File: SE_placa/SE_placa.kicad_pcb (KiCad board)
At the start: 2 copper layers, 118.1 x 58.4 mm, 70 parts, among them IC1 TP4056, J1 5V, J2 Micro_SD_Card_Det_Hirose_DM3AT, J3 Conn_02x07_ESP32_IO, J4 I2C-0, J5 I2C-1, J6 Conn_02x03_LORA_IO, J7 U.FL-R-SMT(01), J8 UART, J9 Connector Bateria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

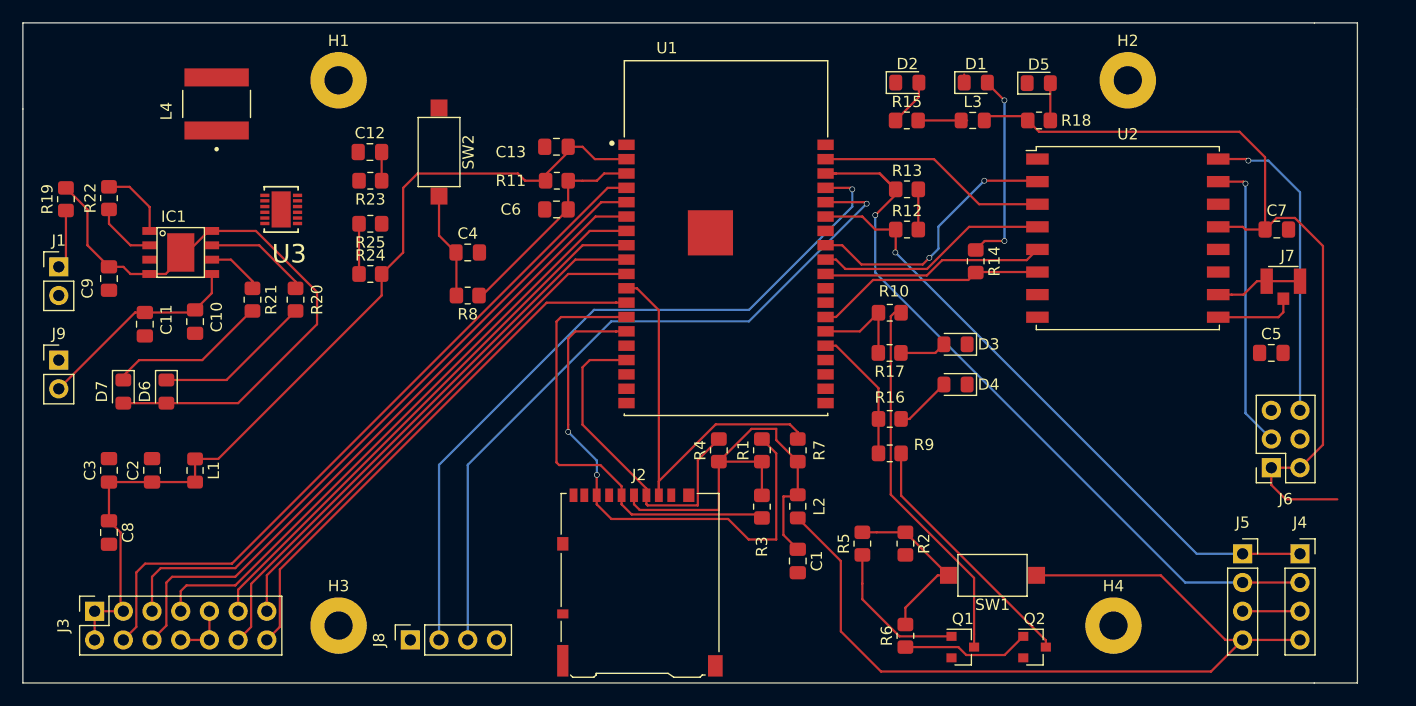
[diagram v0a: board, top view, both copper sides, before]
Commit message: continuacion de ruteo
Solo queda por rutear tierras.
agrego regla de ruteo para el U3 elemento mas pequeño regulador LTC3441, aun siguen generando error la base del elemento.
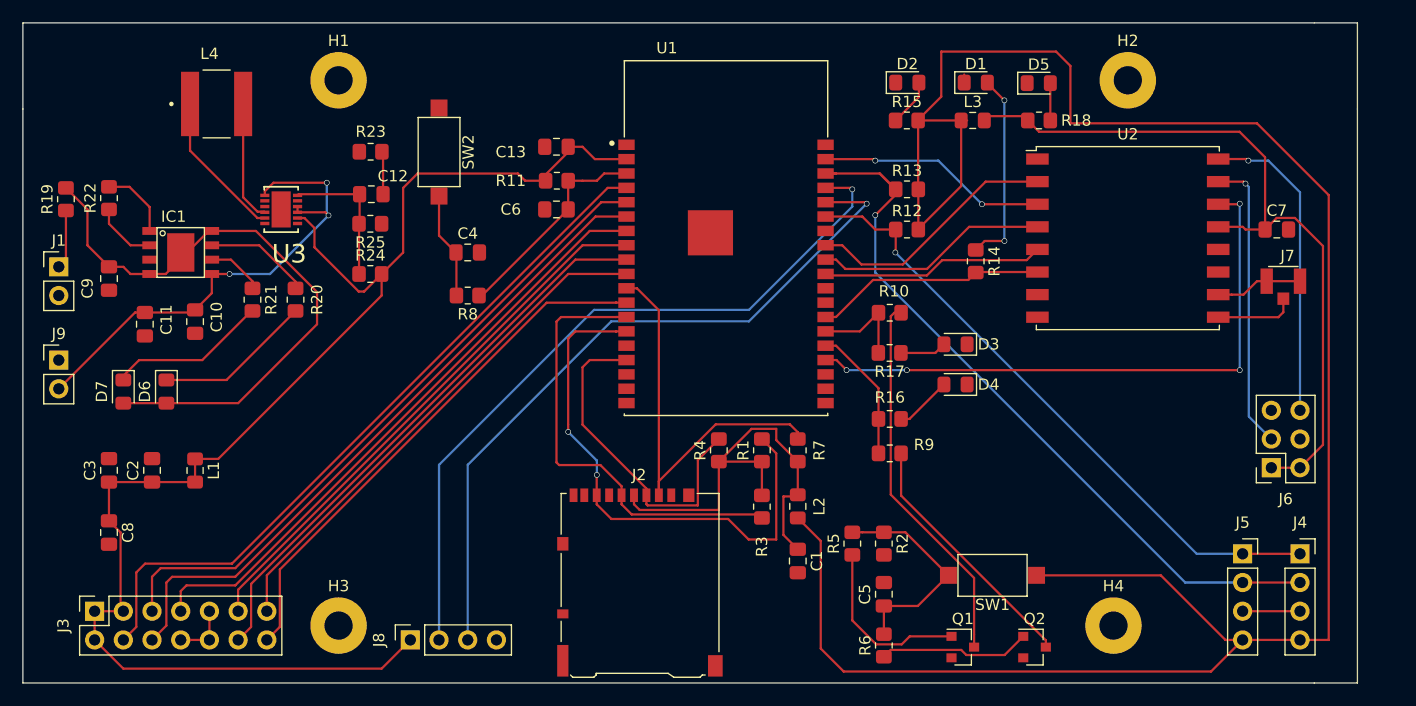
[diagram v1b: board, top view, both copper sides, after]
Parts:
- moved C5 40.4 mm to (177.8, 68.3), turned to 90 degrees
- moved C12 3.74 mm to (132.4, 32.9)
- moved R23 2.57 mm to (132.4, 29.2)
- moved R6 2.09 mm to (177.8, 72.9)
- moved R2 1.91 mm to (177.8, 63.9)
- moved R5 0.89 mm to (175.0, 63.9)
- turned L4 to 0 degrees
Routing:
- net +3V3: track 165.7 -> 318.4 mm
- net Net-(U1-Pad23): track 0.00 -> 53.7 mm, vias 0 -> 4
- net /cargador_regulador/BAT+: track 18.7 -> 43.7 mm, vias 0 -> 3
- net Net-(L4-Pad1): track 0.00 -> 13.2 mm
- net Net-(L4-Pad2): track 0.00 -> 10.7 mm
- net /cargador_regulador/FB: track 4.45 -> 12.6 mm
- net +3.3VP: track 74.5 -> 66.6 mm
- net Net-(C5-Pad1): track 15.7 -> 19.4 mm
- net Net-(Q1-Pad1): track 13.2 -> 15.7 mm
- net Net-(Q2-Pad1): track 11.4 -> 13.5 mm
- net Net-(C12-Pad2): track 2.54 -> 3.80 mm
- net Net-(U1-Pad31): track 23.7 -> 22.5 mm, vias 2 -> 0
- net Net-(U1-Pad37): vias 0 -> 2
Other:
- net class U3 added: clearance 0.2, trace_width 0.2, via_dia 0.4, via_drill 0.3
- rule trace_min: 0.2 -> 0.15

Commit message: ruteo de tierras
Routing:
- net GND: track 25.5 -> 392.2 mm
- net Net-(R23-Pad2): track 0.00 -> 9.23 mm, vias 0 -> 2
- net Net-(U1-Pad23): track 53.7 -> 56.4 mm
- net /cargador_regulador/BAT+: track 43.7 -> 44.6 mm
- net /SPI2-SCK: track 40.0 -> 39.4 mm

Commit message: actualizacion tierra
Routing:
- net GND: track 392.2 -> 442.2 mm, vias 0 -> 4
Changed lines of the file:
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@@
     (thickness 1.6)
     (drawings 8)
-    (tracks 514)
+    (tracks 540)
     (zones 0)
     (modules 70)
@@
   (segment (start 143.51 72.39) (end 147.54 72.39) (width 0.2) (layer F.Cu) (net 1))
   (segment (start 170.18 67.39) (end 162.885 74.685) (width 0.2) (layer F.Cu) (net 1))
-  (segment (start 170.18 66.4425) (end 170.18 67.39) (width 0.2) (layer F.Cu) (net 1))
   (segment (start 170.18 66.4425) (end 164.2325 66.4425) (width 0.2) (layer F.Cu) (net 1))
   (segment (start 161.675 63.885) (end 149.385 63.885) (width 0.2) (layer F.Cu) (net 1))
@@
   (segment (start 153.485 57.6) (end 153.035 57.15) (width 0.2) (layer F.Cu) (net 1))
   (segment (start 153.485 59.585) (end 153.485 57.6) (width 0.2) (layer F.Cu) (net 1))
+  (segment (start 215.265 37.719) (end 213.614 36.068) (width 0.2) (layer F.Cu) (net 1))
+  (segment (start 215.265 40.005) (end 215.265 37.719) (width 0.2) (layer F.Cu) (net 1))
+  (segment (start 214.63 40.64) (end 215.265 40.005) (width 0.2) (layer F.Cu) (net 1))
+  (segment (start 189.535 74.575) (end 190.135 73.975) (width 0.2) (layer F.Cu) (net 1))
+  (segment (start 184.435 74.575) (end 189.535 74.575) (width 0.2) (layer F.Cu) (net 1))
+  (segment (start 183.835 73.975) (end 184.435 74.575) (width 0.2) (layer F.Cu) (net 1))
+  (segment (start 183.785 73.975) (end 183.835 73.975) (width 0.2) (layer F.Cu) (net 1))
+  (via (at 179.705 74.295) (size 0.5) (drill 0.4) (layers F.Cu B.Cu) (net 1))
+  (segment (start 180.025 73.975) (end 179.705 74.295) (width 0.2) (layer F.Cu) (net 1))
+  (segment (start 183.785 73.975) (end 180.025 73.975) (width 0.2) (layer F.Cu) (net 1))
+  (via (at 179.705 67.945) (size 0.5) (drill 0.4) (layers F.Cu B.Cu) (net 1))
+  (segment (start 179.705 74.295) (end 179.705 67.945) (width 0.2) (layer B.Cu) (net 1))
+  (segment (start 178.435 67.945) (end 177.8 67.31) (width 0.2) (layer F.Cu) (net 1))
+  (segment (start 179.705 67.945) (end 178.435 67.945) (width 0.2) (layer F.Cu) (net 1))
+  (via (at 175.26 67.31) (size 0.5) (drill 0.4) (layers F.Cu B.Cu) (net 1))
+  (segment (start 177.8 67.31) (end 175.26 67.31) (width 0.2) (layer F.Cu) (net 1))
+  (via (at 171.45 67.945012) (size 0.5) (drill 0.4) (layers F.Cu B.Cu) (net 1))
+  (segment (start 172.085012 67.31) (end 171.45 67.945012) (width 0.2) (layer B.Cu) (net 1))
+  (segment (start 175.26 67.31) (end 172.085012 67.31) (width 0.2) (layer B.Cu) (net 1))
+  (segment (start 170.815012 67.945012) (end 170.18 67.31) (width 0.2) (layer F.Cu) (net 1))
+  (segment (start 171.45 67.945012) (end 170.815012 67.945012) (width 0.2) (layer F.Cu) (net 1))
+  (segment (start 170.18 67.31) (end 170.18 67.39) (width 0.2) (layer F.Cu) (net 1))
+  (segment (start 170.18 66.4425) (end 170.18 67.31) (width 0.2) (layer F.Cu) (net 1))
+  (segment (start 192.04 43.18) (end 191.39 43.83) (width 0.2) (layer F.Cu) (net 1))
+  (segment (start 205.105 43.18) (end 192.04 43.18) (width 0.2) (layer F.Cu) (net 1))
+  (segment (start 206.455 41.83) (end 205.105 43.18) (width 0.2) (layer F.Cu) (net 1))
+  (segment (start 207.39 41.83) (end 206.455 41.83) (width 0.2) (layer F.Cu) (net 1))
   (segment (start 167.005 59.595) (end 167.005 56.61) (width 0.2) (layer F.Cu) (net 2))
   (segment (start 167.005 56.61) (end 163.195 56.61) (width 0.2) (layer F.Cu) (net 2))
@@
   (segment (start 185.785 66.904998) (end 185.785 71.882001) (width 0.2) (layer F.Cu) (net 25))
   (segment (start 185.785 71.882001) (end 185.785 73.025) (width 0.2) (layer F.Cu) (net 25))
-  (segment (start 179.37899 72.78201) (end 180.086 72.075) (width 0.2) (layer F.Cu) (net 26))
-  (segment (start 177.122176 72.78201) (end 179.37899 72.78201) (width 0.2) (layer F.Cu) (net 26))
-  (segment (start 180.086 72.075) (end 183.785 72.075) (width 0.2) (layer F.Cu) (net 26))
-  (segment (start 175.006 70.665834) (end 177.122176 72.78201) (width 0.2) (layer F.Cu) (net 26))
-  (segment (start 175.006 64.865) (end 175.006 70.665834) (width 0.2) (layer F.Cu) (net 26))
+  (segment (start 175.006 64.865) (end 174.709998 65.161002) (width 0.2) (layer F.Cu) (net 26))
+  (segment (start 174.709998 65.161002) (end 174.709998 70.369832) (width 0.2) (layer F.Cu) (net 26))
+  (segment (start 174.709998 70.369832) (end 177.122176 72.78201) (width 0.2) (layer F.Cu) (net 26))
+  (segment (start 177.122176 72.78201) (end 183.07799 72.78201) (width 0.2) (layer F.Cu) (net 26))
+  (segment (start 183.07799 72.78201) (end 183.785 72.075) (width 0.2) (layer F.Cu) (net 26))
   (segment (start 179.324 59.614) (end 192.135 72.425) (width 0.2) (layer F.Cu) (net 27))
   (segment (start 179.324 55.88) (end 179.324 59.614) (width 0.2) (layer F.Cu) (net 27))
@@
     (polygon
       (pts
-        (xy 205.74 44.45) (xy 193.04 44.45) (xy 193.04 27.94) (xy 205.74 27.94)
+        (xy 205.74 40.64) (xy 193.04 40.64) (xy 193.04 27.94) (xy 205.74 27.94)
       )
     )

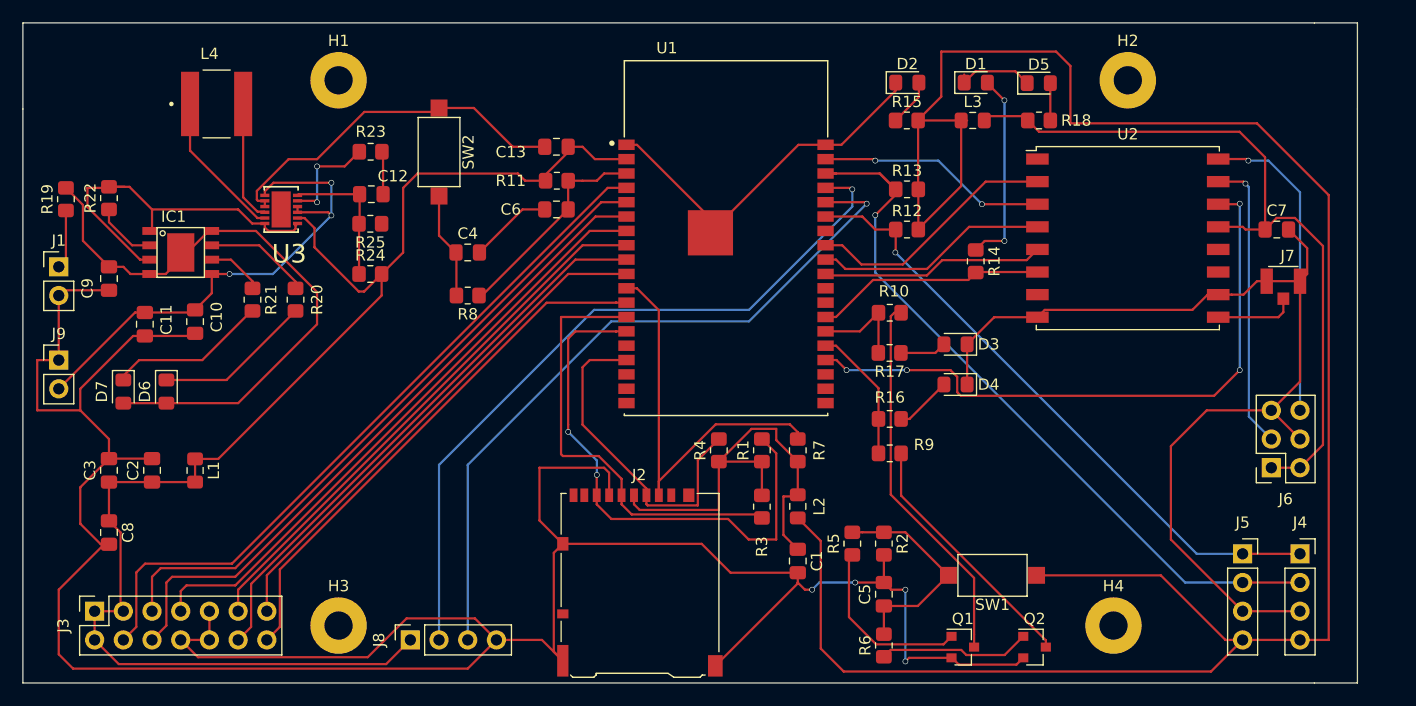
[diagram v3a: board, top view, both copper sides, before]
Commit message: Ruteo 2
Aumento el ancho de las pistas de señales a 0.4 m
aumento las pistas de alimentacion a 1 mm
modifico ubicacion de elementos para mejorar ruteo evitando pasar por debajo de elementos
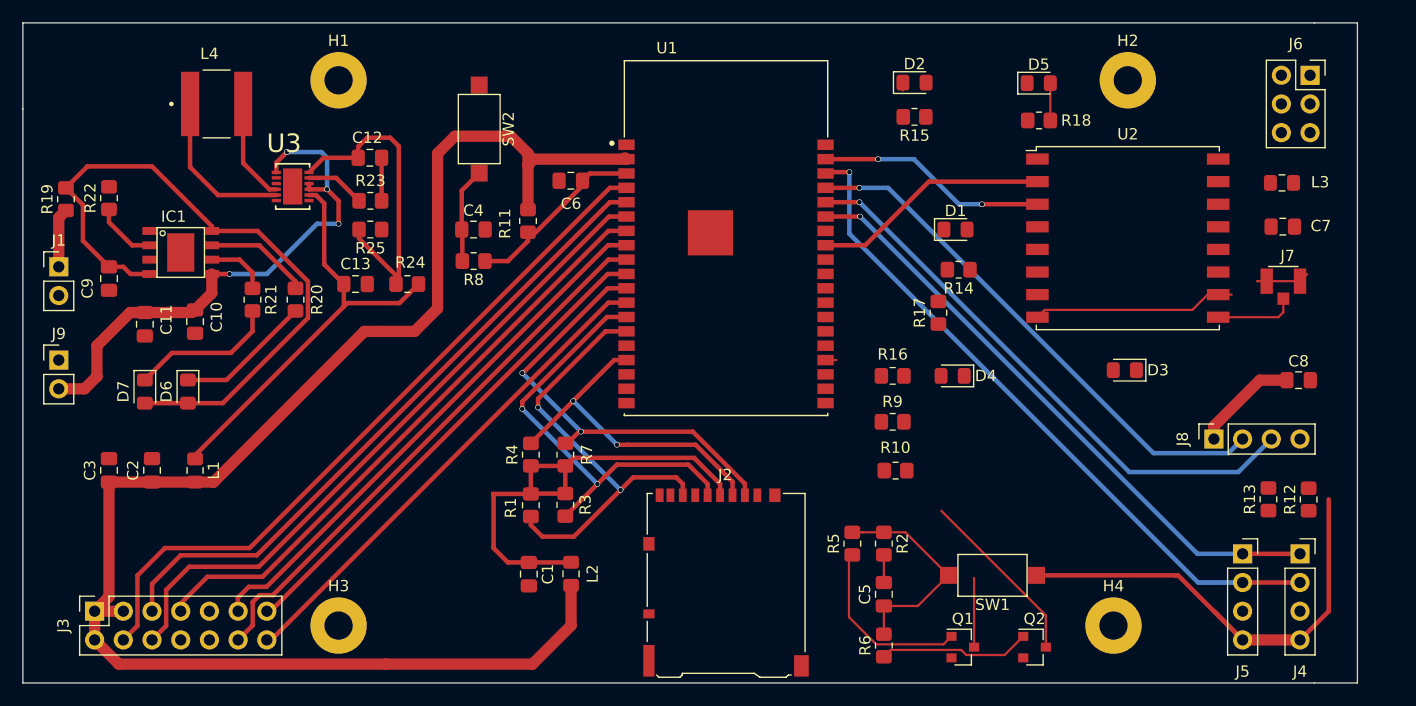
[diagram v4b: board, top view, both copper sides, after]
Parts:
- moved C8 106.1 mm to (214.5, 49.4), turned to 0 degrees
- moved J8 73.3 mm to (207.0, 54.6)
- moved R12 42.8 mm to (215.4, 60.0), turned to 90 degrees
- moved R13 42.1 mm to (211.8, 59.9), turned to 90 degrees
- moved J6 34.9 mm to (215.5, 22.4), turned to 0 degrees
- moved L3 27.9 mm to (213.0, 31.9), turned to 180 degrees
- moved C1 23.8 mm to (146.4, 66.6)
- moved C13 21.5 mm to (131.0, 40.9), turned to 0 degrees
- moved R1 21.0 mm to (146.6, 60.5), turned to 270 degrees
- moved L2 20.9 mm to (150.1, 66.5)
- moved R7 20.6 mm to (149.6, 56.0)
- moved R3 17.4 mm to (149.6, 60.4)
- moved R4 16.6 mm to (146.6, 56.0)
- moved D3 15.2 mm to (199.1, 48.5)
- moved R10 14.0 mm to (178.8, 57.4)
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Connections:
- C13 pad 1: +3V3 -> /cargador_regulador/Vout3.3V
- C7 pad 1: +3.3VP -> Net-(C7-Pad1)
- J6 pad 1: +3.3VP -> +3V3
- J6 pad 2: +3.3VP -> +3V3
- L1 pad 1: +3V3 -> /cargador_regulador/Vout3.3V
- L3 pad 2: +3.3VP -> Net-(C7-Pad1)
- R18 pad 2: +3.3VP -> +3V3
- R24 pad 2: +3V3 -> /cargador_regulador/Vout3.3V
- U2 pad 13: +3.3VP -> Net-(C7-Pad1)
- U3 pad 8: +3V3 -> /cargador_regulador/Vout3.3V
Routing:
- net GND: track 442.2 -> 29.1 mm, vias 4 -> 0
- net +3V3: track 318.1 -> 190.0 mm
- net +3.3VP: track 66.6 -> 0.00 mm
- net Net-(U1-Pad23): track 56.4 -> 0.96 mm, vias 4 -> 0
- net /cargador_regulador/Vout3.3V: track 0.00 -> 37.9 mm
- net /L-DIO2: track 27.8 -> 0.00 mm, vias 1 -> 0
- net Net-(Q1-Pad3): track 33.4 -> 6.12 mm
- net /L-DIO1: track 26.0 -> 0.00 mm, vias 1 -> 0
- net /SPI1-SCK: track 20.6 -> 0.00 mm
- net /SPI1-RST: track 20.4 -> 0.00 mm
- net Net-(U1-Pad29): track 19.8 -> 0.19 mm
- net /TXD0: track 65.5 -> 47.2 mm
- net Net-(D1-Pad2): track 17.5 -> 0.00 mm, vias 2 -> 0
- net /cargador_regulador/FB: track 12.6 -> 28.5 mm
- net /RXD0: track 64.1 -> 50.6 mm
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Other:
- net class Default: trace_width 0.2 -> 0.4
- net class PWR removed
- net class U3 removed
- rule trace_min: 0.15 -> 0.4

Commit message: Update SE_placa.kicad_pcb
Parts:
- moved D3 15.0 mm to (184.2, 48.4)
- moved R10 7.38 mm to (184.4, 52.6), turned to 180 degrees
- moved SW1 4.77 mm to (188.2, 62.0)
- moved D4 4.48 mm to (179.5, 48.4), turned to 0 degrees
- moved R16 3.64 mm to (179.3, 52.6)
- moved R9 3.64 mm to (179.3, 56.6)
- moved R17 1.55 mm to (184.2, 43.7), turned to 0 degrees
- moved R14 0.30 mm to (184.2, 39.5)
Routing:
- net +3V3: track 190.0 -> 262.5 mm
- net /IO0: track 0.00 -> 26.6 mm
- net /SPI1-RST: track 0.00 -> 22.6 mm
- net Net-(Q1-Pad3): track 6.12 -> 21.4 mm, vias 0 -> 2
- net /IO2: track 0.00 -> 13.3 mm
- net /I2C-SCL: track 60.3 -> 73.5 mm
- net /L-DIO1: track 0.00 -> 12.1 mm
- net Net-(Q2-Pad3): track 15.9 -> 26.9 mm, vias 0 -> 2
- net Net-(C5-Pad1): track 19.4 -> 10.3 mm
- net /L-DIO2: track 0.00 -> 6.56 mm
- net Net-(D3-Pad2): track 0.00 -> 4.71 mm
- net Net-(D4-Pad2): track 0.00 -> 4.25 mm
- net /I2C-SDA: track 54.5 -> 58.7 mm
- net Net-(C7-Pad1): track 0.00 -> 3.90 mm
- net Net-(D1-Pad2): track 0.00 -> 3.44 mm
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
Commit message: Update SE_placa.kicad_pcb
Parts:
- moved R7 16.0 mm to (165.6, 55.1), turned to 270 degrees
- moved R3 12.0 mm to (160.4, 55.1)
- moved R5 7.61 mm to (181.0, 68.5)
- moved R1 7.21 mm to (152.9, 57.0), turned to 0 degrees
- moved R4 6.21 mm to (151.9, 52.8)
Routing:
- net Net-(U1-Pad23): track 0.00 -> 54.9 mm, vias 0 -> 4
- net /SPI2-SS: track 38.9 -> 4.00 mm, vias 2 -> 0
- net Net-(U1-Pad29): track 0.19 -> 22.5 mm
- net /SPI1-SCK: track 0.00 -> 21.8 mm
- net GND: track 29.1 -> 8.20 mm
- net +3V3: track 262.5 -> 282.3 mm
- net /SPI2-MISO: track 39.4 -> 22.5 mm
- net Net-(Q1-Pad1): track 16.0 -> 3.81 mm
- net Net-(C5-Pad1): track 10.3 -> 19.4 mm
- net /SPI2-SCK: track 38.6 -> 30.3 mm
- net Net-(C1-Pad1): track 43.1 -> 35.7 mm
- net Net-(C7-Pad1): track 3.90 -> 8.54 mm
- net /SPI2-MOSI: track 29.8 -> 27.0 mm
- net /IO0: track 26.6 -> 25.7 mm

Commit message: Update SE_placa.kicad_pcb
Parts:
- moved D2 30.6 mm to (149.9, 21.8)
- moved R15 30.6 mm to (149.9, 24.8)
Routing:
- net +3V3: track 282.3 -> 311.9 mm, vias 0 -> 2
- net /SPI2-SS: track 4.00 -> 32.7 mm
- net GND: track 8.20 -> 7.50 mm
